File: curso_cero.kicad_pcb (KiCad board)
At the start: 2 copper layers, 53.3 x 49.5 mm, 31 parts, among them P1 CONN_01X06, P2 CONN_01X06, P3 CONN_01X03, P4 CONN_01X04, P5 CONN_01X03, P6 CONN_01X03, P7 CONN_01X08, P8 CONN_01X08, P9 CONN_01X04, SW1 SW_PUSH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

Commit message: Cambios para las nuevas versiones de Kicad. Corregidos fallos estéticos
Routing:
- net PINA3: track 55.5 -> 54.5 mm
- net PINA4: track 58.9 -> 57.8 mm
- net PINA2: track 79.4 -> 78.4 mm
- net PIN6: track 42.3 -> 41.3 mm
- net PIN11: track 22.9 -> 22.2 mm
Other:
- board text added: "https://sindormir.net/curso-cero-programacion https://sindormir.net/oshw-s4a-mini-board"

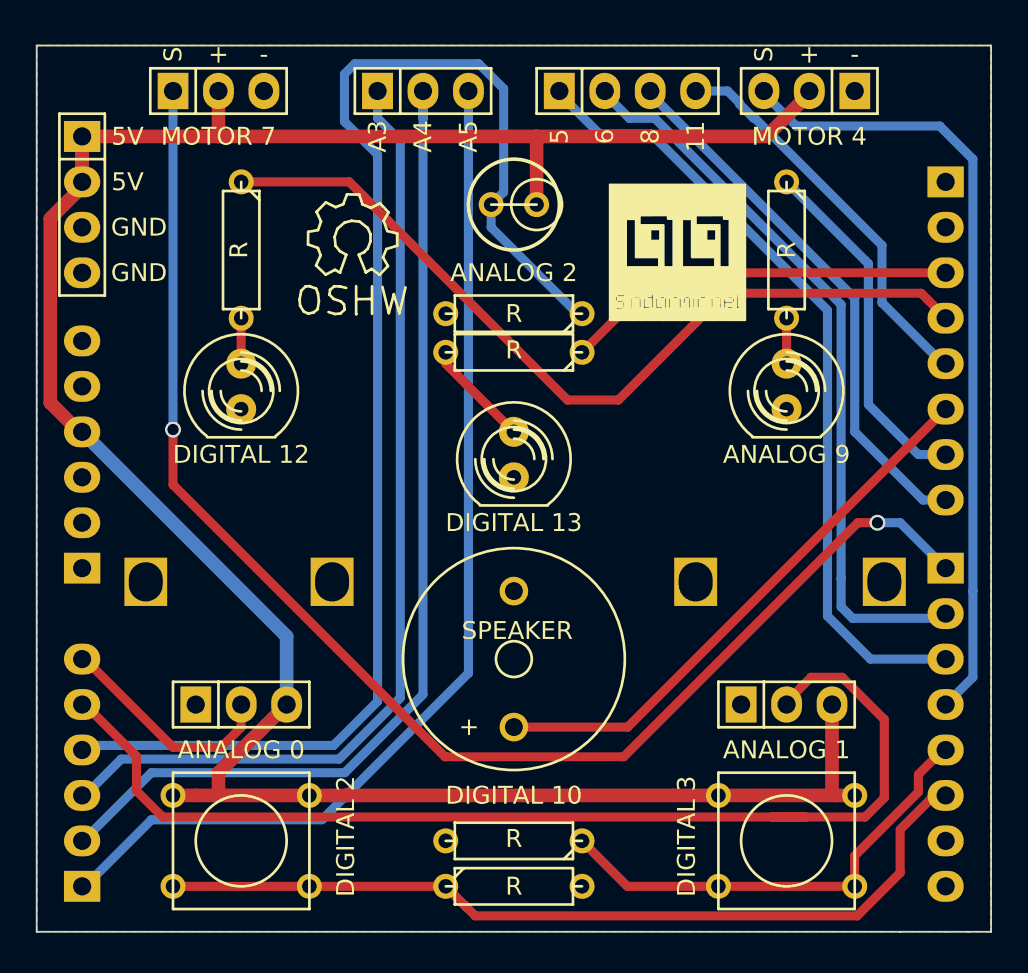
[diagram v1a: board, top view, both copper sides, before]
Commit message: comprobado y recolocada posicion cabeceras Arduino, añadidas cotas en mil, optimizacion de trazado, rellenado recuadro de datos de PCB, editadas clases de nets, reubicados nuevos footprints de boton y potenciometro, corregida polaridad buzzer en serigrafia, recolocadas serigrafías y visibilizadas referencias y valores
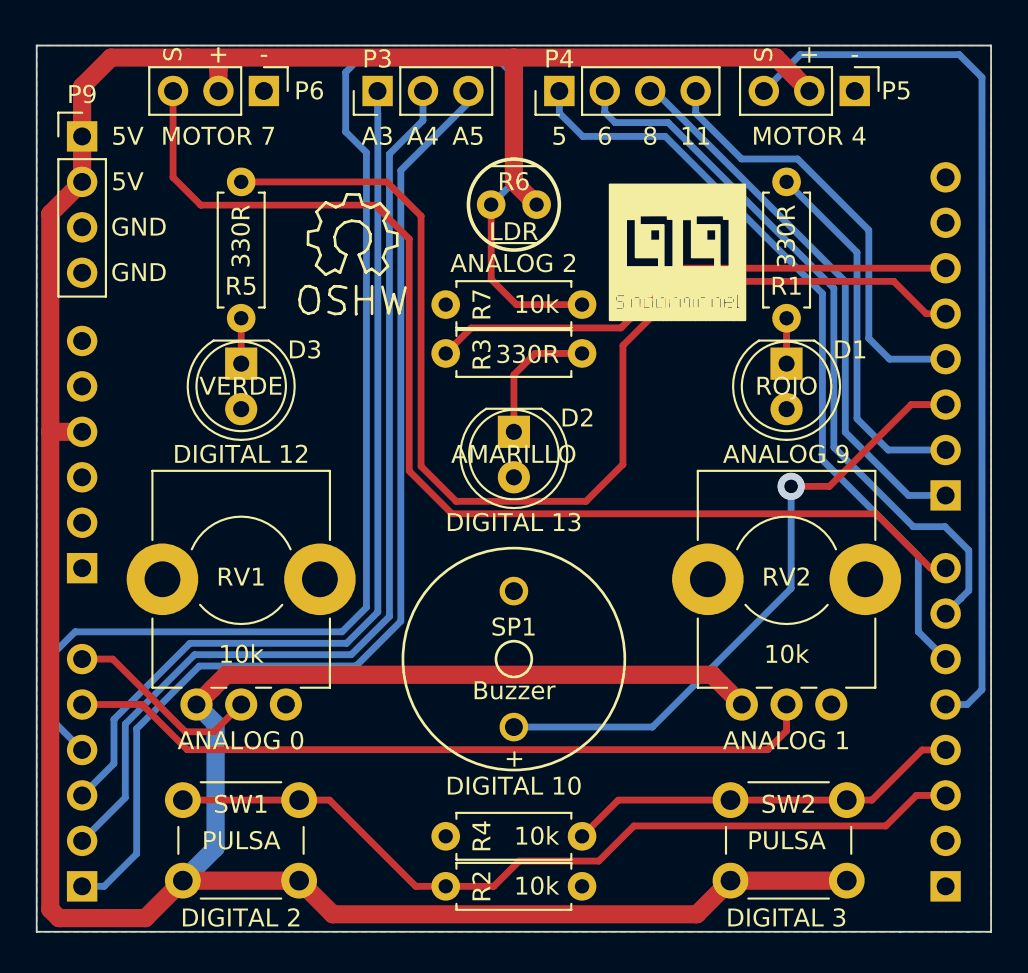
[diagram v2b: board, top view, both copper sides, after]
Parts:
- removed 1pin (x2), ? (x2): VAL**, Connect:1pin
- D1: value LED -> ROJO; footprint LEDs:LED-5MM -> LEDs:LED_D5.0mm
- D2: value LED -> AMARILLO; footprint LEDs:LED-5MM -> LEDs:LED_D5.0mm
- D3: value LED -> VERDE; footprint LEDs:LED-5MM -> LEDs:LED_D5.0mm
- P1: value CONN_01X06 -> Arduino Power header; footprint Pin_Headers:Pin_Header_Straight_1x06 -> Pin_Headers:Pin_Header_Straight_1x06_Pitch2.54mm
- P2: value CONN_01X06 -> Arduino Analog header; footprint Pin_Headers:Pin_Header_Straight_1x06 -> Pin_Headers:Pin_Header_Straight_1x06_Pitch2.54mm
- P3: value CONN_01X03 -> Analog pin; footprint Socket_Strips:Socket_Strip_Straight_1x03 -> Socket_Strips:Socket_Strip_Straight_1x03_Pitch2.54mm
- P4: value CONN_01X04 -> Digital pin; footprint Socket_Strips:Socket_Strip_Straight_1x04 -> Socket_Strips:Socket_Strip_Straight_1x04_Pitch2.54mm
- P5: value CONN_01X03 -> Servo 1; footprint Pin_Headers:Pin_Header_Straight_1x03 -> Pin_Headers:Pin_Header_Straight_1x03_Pitch2.54mm
- P6: value CONN_01X03 -> Servo 2; footprint Pin_Headers:Pin_Header_Straight_1x03 -> Pin_Headers:Pin_Header_Straight_1x03_Pitch2.54mm
- P7: value CONN_01X08 -> Arduino Digital H header; footprint Pin_Headers:Pin_Header_Straight_1x08 -> Pin_Headers:Pin_Header_Straight_1x08_Pitch2.54mm
- P8: value CONN_01X08 -> Arduino Digital L header; footprint Pin_Headers:Pin_Header_Straight_1x08 -> Pin_Headers:Pin_Header_Straight_1x08_Pitch2.54mm
- P9: value CONN_01X04 -> Power; footprint Socket_Strips:Socket_Strip_Straight_1x04 -> Socket_Strips:Socket_Strip_Straight_1x04_Pitch2.54mm
- R1, R3, R5: value R -> 330R; footprint Discret:R3 -> Resistors_ThroughHole:R_Axial_DIN0207_L6.3mm_D2.5mm_P7.62mm_Horizontal
- R2, R4, R7: value R -> 10k; footprint Discret:R3 -> Resistors_ThroughHole:R_Axial_DIN0207_L6.3mm_D2.5mm_P7.62mm_Horizontal
- R6: value R -> LDR; footprint Discret:R1 -> Opto-Devices:Resistor_LDR_4.9x4.2_RM2.54
- RV1, RV2: value POT -> 10k; footprint Pin_Headers:Pin_Header_Straight_1x03 -> Potentiometers:Potentiometer_Alps_RK09K_Horizontal
- SP1: value SPEAKER -> Buzzer
- SW1, SW2: value SW_PUSH -> PULSA; footprint Discret:SW_PUSH_SMALL -> Buttons_Switches_ThroughHole:SW_PUSH_6mm_h5mm
- moved P8 8.89 mm to (163.8, 141.0), turned to 0 degrees
- moved P7 8.64 mm to (163.8, 119.1), turned to 0 degrees
- moved SP1 7.62 mm to (139.7, 124.5), turned to 270 degrees
- moved P1 6.35 mm to (115.6, 123.2), turned to 0 degrees
- moved P2 6.35 mm to (115.6, 141.0), turned to 0 degrees
- moved SW2 4.03 mm to (158.3, 140.7), turned to 180 degrees
- moved SW1 3.93 mm to (127.7, 140.7), turned to 180 degrees
- moved R7 3.84 mm to (143.5, 108.5)
- moved R4 3.82 mm to (143.5, 138.2)
- moved R3 3.81 mm to (143.5, 111.2)
- moved P4 3.81 mm to (142.2, 96.5), turned to 90 degrees
- moved P9 3.81 mm to (115.6, 99.1), turned to 0 degrees
- moved R1 3.81 mm to (154.9, 109.2), turned to 90 degrees
- moved R2 3.81 mm to (135.9, 141.0)
- moved R5 3.81 mm to (124.5, 109.2), turned to 90 degrees
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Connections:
- net 3V3 renamed Net-(P1-Pad5)
- net 5V renamed +5V
- net RESET renamed Net-(P1-Pad6)
- net VIN renamed Net-(P1-Pad1)
- P4 pad 1: PIN5 -> PIND5
- P4 pad 2: PIN6 -> PIND6
- P4 pad 3: PIN8 -> PIND8
- P4 pad 4: PIN11 -> PIND11
- P5 pad 3: PIN4 -> PIND4
- P6 pad 1: PIN7 -> GND
- P6 pad 3: GND -> PIND7
- P7 pad 1: AREF -> PIND8
- P7 pad 2: GND -> PIND9
- P7 pad 3: PIN13 -> PIND10
- P7 pad 4: PIN12 -> PIND11
- P7 pad 5: PIN11 -> PIND12
- P7 pad 6: PIN10 -> PIND13
- P7 pad 7: PIN9 -> GND
- P7 pad 8: PIN8 -> Net-(P7-Pad8)
- P8 pad 1: PIN7 -> Net-(P8-Pad1)
- P8 pad 2: PIN6 -> Net-(P8-Pad2)
- P8 pad 3: PIN5 -> PIND2
- P8 pad 4: PIN4 -> PIND3
- P8 pad 5: PIN3 -> PIND4
- P8 pad 6: PIN2 -> PIND5
- P8 pad 7: PIN1 -> PIND6
- P8 pad 8: PIN0 -> PIND7
- R1 pad 1: PIN9 -> Net-(D1-Pad1)
- R1 pad 2: Net-(D1-Pad1) -> PIND9
- R2 pad 1: PIN2 -> PIND2
- R3 pad 1: PIN13 -> Net-(D2-Pad1)
- R3 pad 2: Net-(D2-Pad1) -> PIND13
- R4 pad 1: PIN3 -> PIND3
- R5 pad 1: PIN12 -> Net-(D3-Pad1)
- R5 pad 2: Net-(D3-Pad1) -> PIND12
- SP1 pad 1: PIN10 -> GND
- SP1 pad 2: GND -> PIND10
- SW1 pad 2: PIN2 -> PIND2
- SW2 pad 2: PIN3 -> PIND3
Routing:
- net PIN7: track 78.0 -> 0.00 mm, vias 2 -> 0
- net PIND12: track 0.00 -> 64.7 mm
- net PIND7: track 0.00 -> 64.7 mm
- net +5V: track 139.3 -> 191.2 mm
- net PIND4: track 0.00 -> 50.2 mm
- net PIN2: track 48.5 -> 0.00 mm
- net PIN12: track 47.6 -> 0.00 mm
- net PIND2: track 0.00 -> 46.7 mm
- net PIN5: track 45.4 -> 0.00 mm
- net PIN4: track 44.5 -> 0.00 mm
- net PIND5: track 0.00 -> 43.8 mm
- net PIN6: track 41.3 -> 0.00 mm
- net PIND6: track 0.00 -> 41.0 mm
- net PIND10: track 0.00 -> 34.9 mm, vias 0 -> 1
- net PIN10: track 31.6 -> 0.00 mm
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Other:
- net class Default: trace_width 0.508 -> 0.381; via_dia 0.889 -> 1.524; via_drill 0.635 -> 0.762
- net class power: trace_width 0.762 -> 1.016; via_dia 0.889 -> 2.032; via_drill 0.635 -> 1.016
- board text added: "https://sindormir.net/curso-cero-programacion"
- board text added: "https://sindormir.net/oshw-s4a-mini-board"
- board text removed: "https://sindormir.net/curso-cero-programacion https://sindormir.net/oshw-s4a-mini-board"
